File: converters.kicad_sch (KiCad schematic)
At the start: 27 parts, among them U10 TLV3502AIDR, U4 TLV3502AIDR, U5 MCP4728, U6 TLV3502AIDR, U7 TLV3502AIDR, U8 MCP4728, U9 TLV3502AIDR

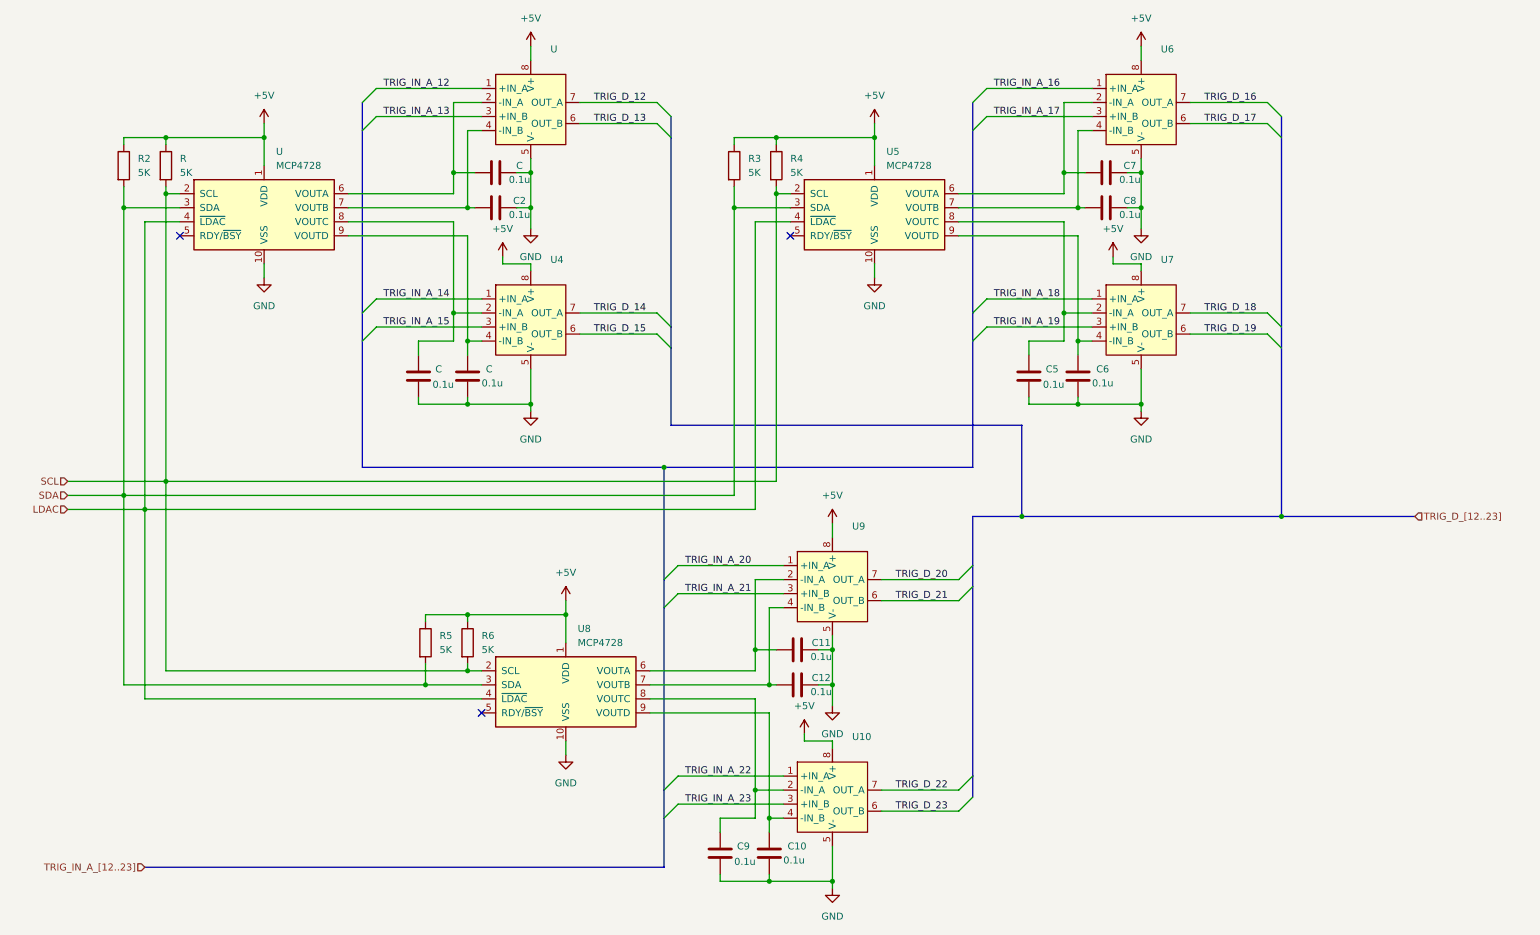
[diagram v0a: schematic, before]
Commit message: Added SD card readers and USB-C for power in.
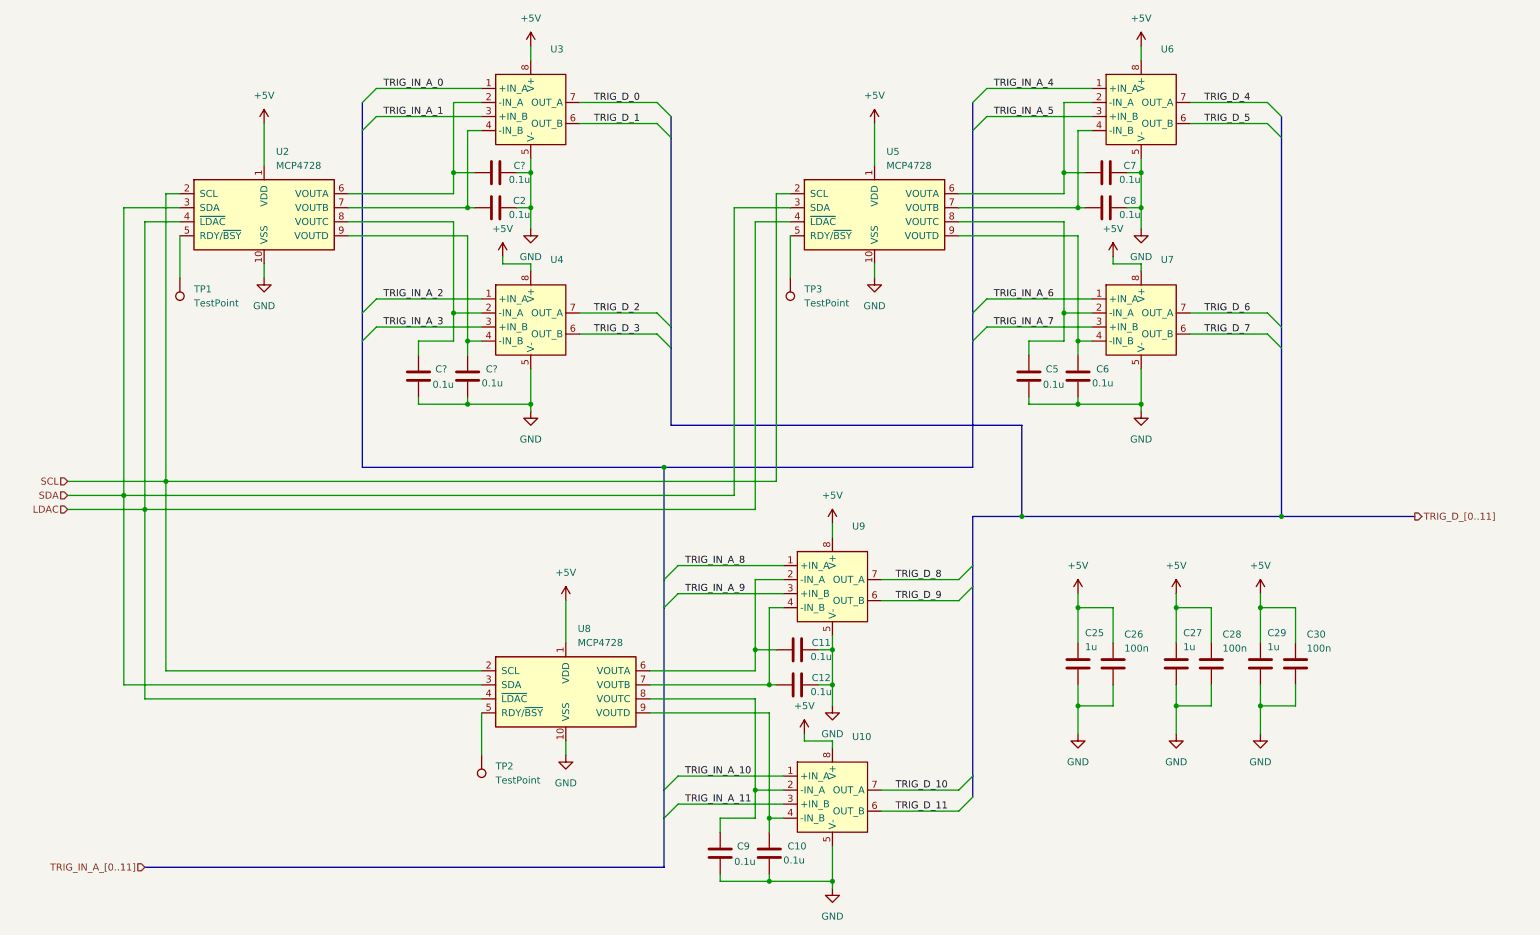
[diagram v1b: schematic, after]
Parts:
- removed R, R2, R3, R4, R5, R6: 5K, symbol Device:R
- added C25, C27, C29: 1u, symbol Device:C
- added C26, C28, C30: 100n, symbol Device:C
- added TP1, TP2, TP3: TestPoint, symbol Connector:TestPoint
- renumbered C to C?, U to U2, U to U3
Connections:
- net +5V: now also C25.1, C26.1, C27.1, C28.1, C29.1, C30.1
- net GND: now also C25.2, C26.2, C27.2, C28.2, C29.2, C30.2
- net at U5.5 (RDY/~{BSY}): now also TP3.1
- net at U2.5 (RDY/~{BSY}): now also TP1.1
- net at U8.5 (RDY/~{BSY}): now also TP2.1
- net TRIG_D_12 renamed TRIG_D_0
- net TRIG_D_13 renamed TRIG_D_1
- net TRIG_D_14 renamed TRIG_D_2
- net TRIG_D_15 renamed TRIG_D_3
- net TRIG_D_16 renamed TRIG_D_4
- net TRIG_D_17 renamed TRIG_D_5
- net TRIG_D_18 renamed TRIG_D_6
- net TRIG_D_19 renamed TRIG_D_7
- net TRIG_D_20 renamed TRIG_D_8
- net TRIG_D_21 renamed TRIG_D_9
- net TRIG_D_22 renamed TRIG_D_10
- net TRIG_D_23 renamed TRIG_D_11
- net TRIG_IN_A_12 renamed TRIG_IN_A_0
- net TRIG_IN_A_13 renamed TRIG_IN_A_1
- net TRIG_IN_A_14 renamed TRIG_IN_A_2
- net TRIG_IN_A_15 renamed TRIG_IN_A_3
- net TRIG_IN_A_16 renamed TRIG_IN_A_4
- net TRIG_IN_A_17 renamed TRIG_IN_A_5
- net TRIG_IN_A_18 renamed TRIG_IN_A_6
- net TRIG_IN_A_19 renamed TRIG_IN_A_7
- net TRIG_IN_A_20 renamed TRIG_IN_A_8
- net TRIG_IN_A_21 renamed TRIG_IN_A_9
- net TRIG_IN_A_22 renamed TRIG_IN_A_10
- net TRIG_IN_A_23 renamed TRIG_IN_A_11
- no-connect marks 3 -> 0

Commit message: Small aesthetic changes and small rework of power sheet.
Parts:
- gave numbers to parts that had none: 1
- renumbered C25 to C?, C26 to C?, TP1 to TP?, U3 to U?, U2 to U?
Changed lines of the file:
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@@
 		(dnp no)
 		(fields_autoplaced yes)
-		(property "Reference" "#PWR050"
+		(property "Reference" "#PWR?"
 			(at 203.2 123.19 0)
 			(effects
@@
 		)
 		(instances
-			(project ""
+			(project "digital"
 				(path "/4c5c7ce5-09d6-4a32-b2a0-f32b0c47f27d/cd76c381-0dc6-471f-8cb4-588b98dd6605"
-					(reference "#PWR050")
+					(reference "#PWR?")
 					(unit 1)
 				)
@@
 		(dnp no)
 		(fields_autoplaced yes)
-		(property "Reference" "TP1"
+		(property "Reference" "TP?"
 			(at 43.18 64.2619 0)
 			(effects
@@
 		)
 		(instances
-			(project ""
+			(project "digital"
 				(path "/4c5c7ce5-09d6-4a32-b2a0-f32b0c47f27d/cd76c381-0dc6-471f-8cb4-588b98dd6605"
-					(reference "TP1")
+					(reference "TP?")
 					(unit 1)
 				)
@@
 		(on_board yes)
 		(dnp no)
-		(property "Reference" "U3"
+		(property "Reference" "U?"
 			(at 107.696 20.828 0)
 			(effects
@@
 		)
 		(instances
-			(project ""
+			(project "digital"
 				(path "/4c5c7ce5-09d6-4a32-b2a0-f32b0c47f27d/cd76c381-0dc6-471f-8cb4-588b98dd6605"
-					(reference "U3")
+					(reference "U?")
 					(unit 1)
 				)
@@
 		(on_board yes)
 		(dnp no)
-		(property "Reference" "C25"
+		(property "Reference" "C?"
 			(at 204.47 126.492 0)
 			(effects
@@
 		)
 		(instances
-			(project ""
+			(project "digital"
 				(path "/4c5c7ce5-09d6-4a32-b2a0-f32b0c47f27d/cd76c381-0dc6-471f-8cb4-588b98dd6605"
-					(reference "C25")
+					(reference "C?")
 					(unit 1)
 				)
@@
 		(on_board yes)
 		(dnp no)
-		(property "Reference" "C26"
+		(property "Reference" "C?"
 			(at 211.582 126.746 0)
 			(effects
@@
 		)
 		(instances
-			(project ""
+			(project "digital"
 				(path "/4c5c7ce5-09d6-4a32-b2a0-f32b0c47f27d/cd76c381-0dc6-471f-8cb4-588b98dd6605"
-					(reference "C26")
+					(reference "C?")
 					(unit 1)
 				)
@@
 		(dnp no)
 		(fields_autoplaced yes)
-		(property "Reference" "#PWR051"
+		(property "Reference" "#PWR?"
 			(at 203.2 151.13 0)
 			(effects
@@
 		)
 		(instances
-			(project ""
+			(project "digital"
 				(path "/4c5c7ce5-09d6-4a32-b2a0-f32b0c47f27d/cd76c381-0dc6-471f-8cb4-588b98dd6605"
-					(reference "#PWR051")
+					(reference "#PWR?")
 					(unit 1)
 				)
@@
 		(on_board yes)
 		(dnp no)
-		(property "Reference" "C?"
+		(property "Reference" "C1"
 			(at 102.108 41.91 90)
 			(effects
@@
 			(project "digital"
 				(path "/4c5c7ce5-09d6-4a32-b2a0-f32b0c47f27d/cd76c381-0dc6-471f-8cb4-588b98dd6605"
-					(reference "C?")
+					(reference "C1")
 					(unit 1)
 				)
@@
 		(dnp no)
 		(fields_autoplaced yes)
-		(property "Reference" "U2"
+		(property "Reference" "U?"
 			(at 58.0233 39.37 0)
 			(effects
@@
 		)
 		(instances
-			(project ""
+			(project "digital"
 				(path "/4c5c7ce5-09d6-4a32-b2a0-f32b0c47f27d/cd76c381-0dc6-471f-8cb4-588b98dd6605"
-					(reference "U2")
+					(reference "U?")
 					(unit 1)
 				)
